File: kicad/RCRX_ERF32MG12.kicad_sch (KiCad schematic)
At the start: 98 parts

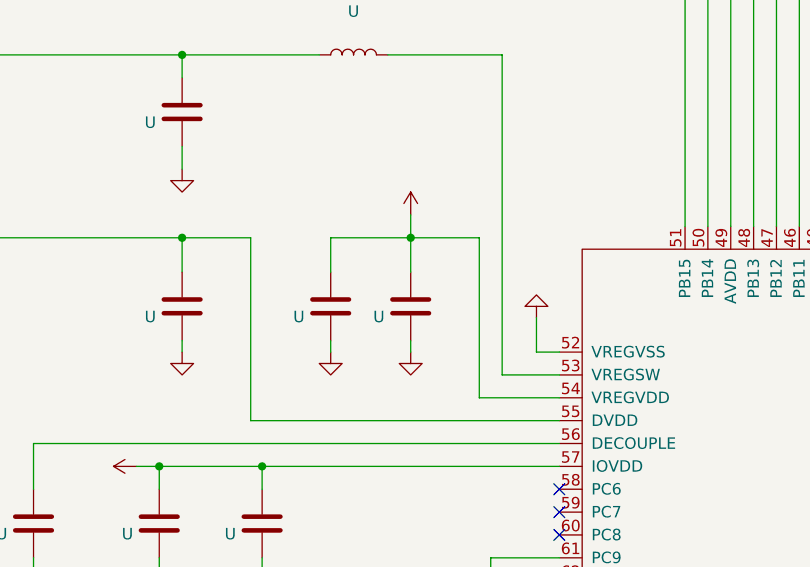
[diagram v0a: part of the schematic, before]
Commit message: Adding PIB USB BRIDGE UML state diagrams
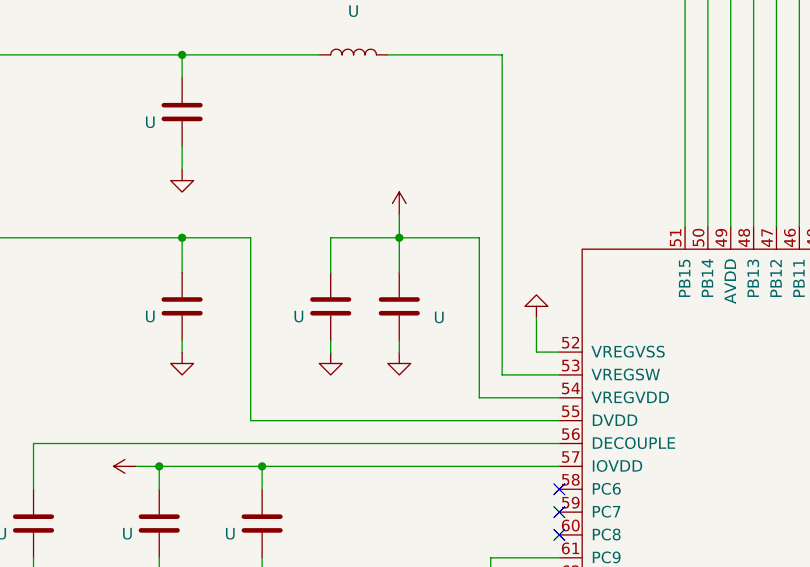
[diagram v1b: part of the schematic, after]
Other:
- moved on the sheet: U

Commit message: Adding PIB USB BRIDGE UML state diagrams - WIP
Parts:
- removed J: Conn_01x02, symbol Connector_Generic:Conn_01x02
- removed U: (no value), symbol device:C
- removed U: (no value), symbol device:R
- added J1: BUZZER, symbol Connector_Generic:Conn_01x02
- C? (x3): renamed from U; value (none) -> 13p
- C? (x2): renamed from U; value (none) -> 33p
- C? (x2): renamed from U; value (none) -> 43p
- C? (x2): renamed from U; value (none) -> 2.2p
- C?: renamed from U; value (none) -> 1p
- C?: renamed from U; value (none) -> 3p
- C? (x8): renamed from U; value (none) -> 100n
- C? (x2): renamed from U; value (none) -> 56p
- C? (x2): renamed from U; value (none) -> 10p
- C?, L?: renamed from U; value (none) -> 220n
- C? (x3), L?: renamed from U; value (none) -> 4u7
- C? (x6): renamed from U; value (none) -> 1u
- C? (x2): renamed from U; value (none) -> 10u
- C?: renamed from U; value (none) -> 10n
- C? (x2): renamed from U; value (none) -> 1n
- C? (x6): renamed from U; value (none) -> 100p
- C? (x2): renamed from U; value (none) -> 68p
- D?: renamed from U; value (none) -> D_Schottky
- HEX_SW?: renamed from U; value (none) -> RF_BAND_SEL
- HEX_SW?: renamed from U; value (none) -> MODEL_ID
- J?: renamed from U; value (none) -> USB_OTG
- J?: renamed from U; value (none) -> Micro_SD_Card
- J?: renamed from U; value (none) -> 50 Ohm 430-460 MHz Antenna
- J?: renamed from U; value (none) -> 50 Ohm 13-79 MHz Antenna
- J?: renamed from U; value (none) -> 50 Ohm 2.4 GHz Antenna
- L?: renamed from U; value (none) -> CBF102WB
- L? (x2): renamed from U; value (none) -> 390n
- L? (x2): renamed from U; value (none) -> 3n
- L? (x2): renamed from U; value (none) -> 62n
- L?: renamed from U; value (none) -> 130n
- L? (x2): renamed from U; value (none) -> 82n
- L? (x2): renamed from U; value (none) -> 470n
- L? (x2): renamed from U; value (none) -> BLM18AG601SN1
- L? (x2): renamed from U; value (none) -> L
- L? (x3): renamed from U; value (none) -> 180n
- L?: renamed from U; value (none) -> 36n
- P?: renamed from U; value (none) -> I2C_BUS
- P?: renamed from U; value (none) -> BATT
- P?: renamed from U; value (none) -> CRSF_BUS
- P?: renamed from U; value (none) -> Nokia 5110 display
- Q?: renamed from U; value (none) -> Q_PMOS_DGS
- R?: renamed from U; value (none) -> 100k
- R?: renamed from U; value (none) -> 1R
- SW?: renamed from U; value (none) -> RESET
- U?: renamed from U; value (none) -> EFR32MG12P433F1024GM48; footprint (none) -> Footprint
- U?: renamed from U; value (none) -> PIC16(L)F1459-I_ML
- U?: renamed from U; value (none) -> LM1117-5.0
- U?: renamed from U; value (none) -> LM1117-3.3
- U? (x2): renamed from U; value (none) -> TLV70245_SOT23-5; footprint (none) -> TO_SOT_Packages_SMD:SOT-23-5
- U? (x2): renamed from U; value (none) -> MAX2650; footprint (none) -> smd-semi:SOT-143
- U?: renamed from U; value (none) -> ADE-1+; footprint (none) -> RF_Mini-Circuits:Mini-Circuits_CD542_LandPatternPL-052
- Y?: renamed from U; value (none) -> 38.400 MHz
- Y?: renamed from U; value (none) -> 514CCAXXXXXXCAG; footprint (none) -> Si500D
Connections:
- net +3V3: now also J?.4 (VDD), P?.1 (Pin_1)
- net BUZZER: now also U?.12 (RC1), U?.59 (PC7), J1.1 (Pin_1)
- net GND: now also J1.2 (Pin_2)
- net /SD_CE: now also U?.60 (PC8); no longer U?.61 (PC9)
- net at J?.2 (D-), U?.15 (D-): no longer U?.12 (RC1)
- net at J?.3 (D+), U?.16 (D+): no longer U?.13 (RC0)
- net at C?.2, U?.14 (Vusb3v3): no longer J?.4 (VDD), P?.1 (Pin_1)
- net /LCD_RESET: now reaches P?.11 (Pin_11)
- net /LCD_RESET: now also U?.13 (RC0), U?.61 (PC9)
- no-connect marks 7 -> 5
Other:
- note added: "USB Adapter for: CMSIS-DAP / COM port / Mass storage (SD Card)"
- moved on the sheet: C?, D?, J?, P?, Q?, R?, SW?, U?

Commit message: Adding PIB USB BRIDGE UML state diagrams - WIP
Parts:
- removed C? (x2): 33p, symbol device:C
- removed C? (x2): 43p, symbol device:C
- removed C? (x2): 2.2p, symbol device:C
- removed C?: 1p, symbol device:C
- removed C? (x2): 56p, symbol device:C
- removed C? (x2): 68p, symbol device:C
- removed D?: D_Schottky, symbol device:D_Schottky
- removed J1: BUZZER, symbol Connector_Generic:Conn_01x02
- removed J?: USB_OTG, symbol conn:USB_OTG
- removed J?: Micro_SD_Card, symbol conn:Micro_SD_Card
- removed L? (x2): 3n, symbol device:L
- removed L? (x2): 62n, symbol device:L
- removed L?: 130n, symbol device:L
- removed L? (x2): 82n, symbol device:L
- removed L? (x3): 180n, symbol device:L
- removed P?: Nokia 5110 display, symbol conn:Conn_02x06_Odd_Even
- removed Q?: Q_PMOS_DGS, symbol device:Q_PMOS_DGS
- removed R?: 100k, symbol device:R
- removed SW?: RESET, symbol RCTX-rescue:SW_Push-switches
- removed U?: PIC16(L)F1459-I_ML, symbol PIC_USB_BRIDGE:PIC16(L)F1459-I_ML
- added C1, C2: 33p, symbol device:C
- added D1: D_Schottky, symbol device:D_Schottky
- added J21: BUZZER, symbol Connector_Generic:Conn_01x02
- added J22: USB_OTG, symbol conn:USB_OTG
- added P1: Nokia 5110 display, symbol conn:Conn_02x06_Odd_Even
- added P?: SD Card, symbol conn:Conn_02x05_Odd_Even
- added Q1: Q_PMOS_DGS, symbol device:Q_PMOS_DGS
- added R1: 100k, symbol device:R
- added SW1: RESET, symbol RCTX-rescue:SW_Push-switches
- added U1: PIC16(L)F1459-I_ML, symbol PIC_USB_BRIDGE:PIC16(L)F1459-I_ML
- added U?: RLP-83+, symbol RF:RLP-83+
- added U?: RBP-440+, symbol RF:RBP-440+
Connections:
- net +3V3: now also P1.1 (Pin_1), P?.1 (Pin_1)
- net +5V: now also Q1.1 (D)
- net BUZZER: now also U?.63 (PC11), J21.1 (Pin_1), U1.20 (RA4); no longer U?.48 (PB13), U?.59 (PC7)
- net GND: now also C1.1, C2.2, J21.2 (Pin_2), J22.6 (Shield), P1.10 (Pin_10), P1.12 (Pin_12), P1.2 (Pin_2), P1.4 (Pin_4), P1.6 (Pin_6), P1.8 (Pin_8), P?.10 (Pin_10), P?.2 (Pin_2), P?.4 (Pin_4), P?.6 (Pin_6), P?.8 (Pin_8), R1.2, SW1.2, U1.17 (VSS), U?.1 (GND), U?.1 (GND), U?.2 (GND), U?.2 (GND), U?.3 (GND), U?.3 (GND), U?.5 (GND), U?.5 (GND), U?.6 (GND), U?.6 (GND), U?.7 (GND), U?.7 (GND)
- net LCD_D/C: now also P1.9 (Pin_9), U1.13 (RC0); no longer U?.63 (PC11)
- net SCK: now also P1.7 (Pin_7), P?.7 (Pin_7), U1.8 (SCK)
- net SDI: now also P?.5 (Pin_5), U1.10 (SDI)
- net SDO: now also P1.5 (Pin_5), P?.3 (Pin_3), U1.6 (SDO)
- net SOC_RESETn: now also U1.5 (RC6)
- net SWCLK: now also U1.2 (RC5)
- net SWDIO: now also U1.3 (RC4)
- net SWO: now also U1.4 (RC3)
- net USB_RX: now also U1.9 (RX)
- net USB_TX: now also U1.7 (TX)
- net /LCD_CE: now also P1.3 (Pin_3), U1.12 (RC1); no longer U?.62 (PC10)
- net /LCD_RESET: now also P1.11 (Pin_11), U1.19 (RA5); no longer U?.61 (PC9)
- net /SD_CE: now also P?.9 (Pin_9), U1.11 (RC2); no longer U?.60 (PC8)
- net at J?.1 (In): now also U?.4 (RF) (x2)
- net at C?.1, C?.2: now also U?.8 (RF), U?.8 (RF)
- new net: D1.2 (A), J22.5 (GND), Q1.2 (G), R1.1
- new net: J22.1 (VBUS), SW1.1, U1.1 (Vpp)
- new net: C1.2, U1.14 (Vusb3v3)
- new net: J22.2 (D-), U1.15 (D-)
- new net: J22.3 (D+), U1.16 (D+)
- new net: C2.1, D1.1 (K), Q1.3 (S), U1.18 (VDD)
- no-connect marks 5 -> 8
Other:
- note added: "- UART bridge for SD card and Nokia 5110 LCD - USB Adapter for: CMSIS-DAP / COM port / Mass storage (SD Card)"
- note added: "2.4 GHz band filter"
- note added: "HF/VHF band filter"
- note added: "RX and TX frontend power"
- note added: "SDO"
- note added: "SD_CARD SS/CS"
- note added: "Sub-GHz multiband 110 MHz up-down converter, pre-amp and power-amp RF MHz ± LO MHz -> IF MHz ------------------------ 10 ... 80 + 110 -> 120-190 430 ... 460 - 110 -> 320-350"
- note added: "UHF band filter"
- note removed: "High Band harmonics suppressor 5th order Chebyshev band pass filter fc: 400-500 MHz"
- note removed: "Low Band harmonics suppressor 9th order Chebyshev low pass filter fc: 80 MHz"
- note removed: "USB Adapter for: CMSIS-DAP / COM port / Mass storage (SD Card)"
- moved on the sheet: C?, J?, L?, U?, Y?

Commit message: Adding PIC docs
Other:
- note added: "- UART bridge for SD card and Nokia 5110 LCD - USB Adapter for: CMSIS-DAP / COM port / MSD (SD Card)"
- note removed: "- UART bridge for SD card and Nokia 5110 LCD - USB Adapter for: CMSIS-DAP / COM port / Mass storage (SD Card)"
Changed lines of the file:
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@@
     (stroke (width 0) (type default))
   )
-  (wire (pts (xy 153.67 229.87) (xy 168.91 229.87))
+  (wire (pts (xy 153.67 229.87) (xy 167.64 229.87))
     (stroke (width 0) (type default))
   )
@@
     (stroke (width 0) (type default))
   )
-  (wire (pts (xy 153.67 234.95) (xy 168.91 234.95))
+  (wire (pts (xy 153.67 234.95) (xy 167.64 234.95))
     (stroke (width 0) (type default))
   )
@@
     (effects (font (size 1.27 1.27)) (justify left bottom))
   )
-  (text "- UART bridge for SD card and Nokia 5110 LCD\n- USB Adapter for: CMSIS-DAP / COM port / Mass storage (SD Card)"
+  (text "- UART bridge for SD card and Nokia 5110 LCD\n- USB Adapter for: CMSIS-DAP / COM port / MSD (SD Card)"
     (at 13.97 194.31 0)
     (effects (font (size 1.27 1.27)) (justify left bottom))
@@
     )
   )
-  (global_label "USB_RX" (shape input) (at 168.91 229.87 0)
-    (effects (font (size 1.27 1.27)) (justify left))
-    (property "Intersheetrefs" "${INTERSHEET_REFS}" (at 8.89 -2.54 0)
+  (global_label "USB_RX" (shape input) (at 167.64 229.87 0)
+    (effects (font (size 1.27 1.27)) (justify left))
+    (property "Intersheetrefs" "${INTERSHEET_REFS}" (at 7.62 -2.54 0)
       (effects (font (size 1.27 1.27)) hide)
     )
@@
     )
   )
-  (global_label "USB_TX" (shape output) (at 168.91 234.95 0)
-    (effects (font (size 1.27 1.27)) (justify left))
-    (property "Intersheetrefs" "${INTERSHEET_REFS}" (at 8.89 7.62 0)
-      (effects (font (size 1.27 1.27)) hide)
-    )
+  (global_label "USB_TX" (shape output) (at 167.64 234.95 0)
+    (effects (font (size 1.27 1.27)) (justify left))
+    (property "Intersheetrefs" "${INTERSHEET_REFS}" (at 7.62 7.62 0)
+      (effects (font (size 1.27 1.27)) hide)
+    )

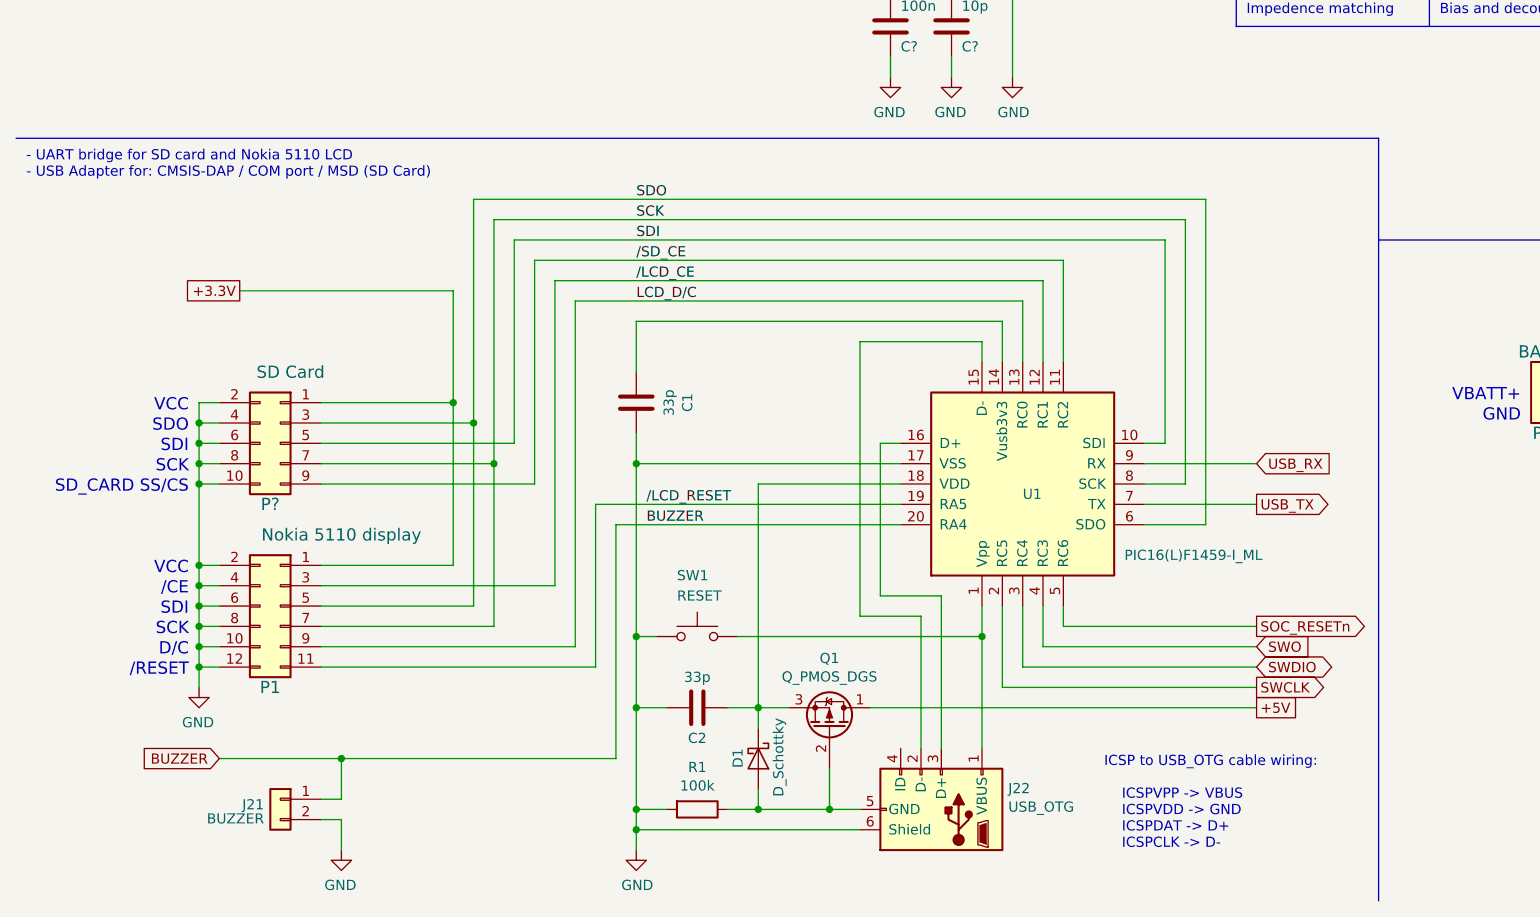
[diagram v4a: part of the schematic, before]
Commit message: Reset PIC by cutting off Vdd via a n/c SW instead of grounding the USB VBUS on Vpp via a n/o SW
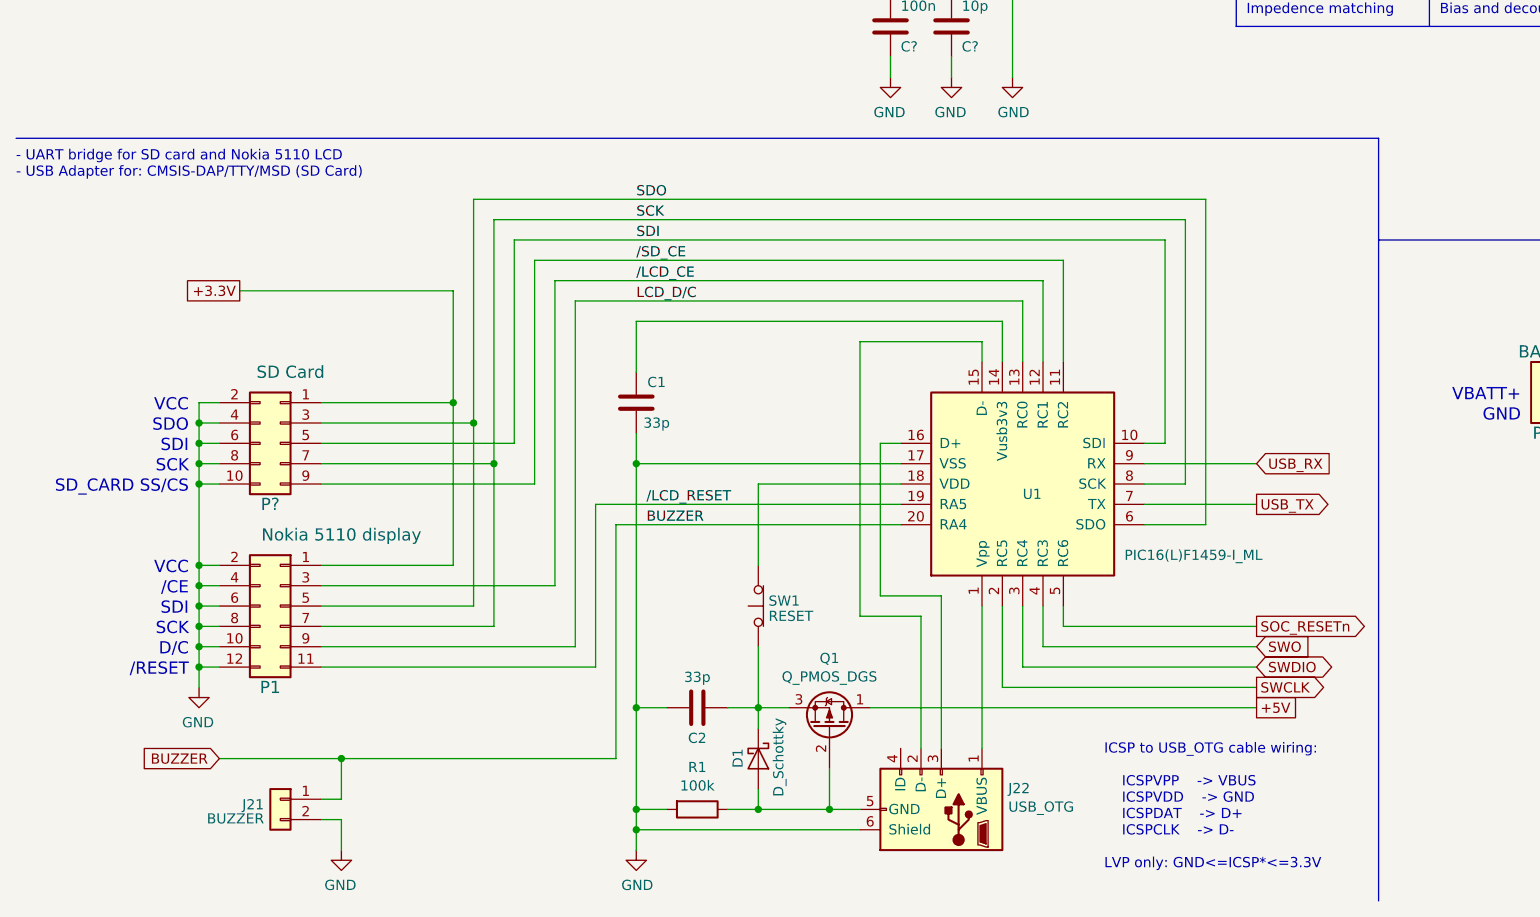
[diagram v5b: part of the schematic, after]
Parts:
- removed SW1: RESET, symbol RCTX-rescue:SW_Push-switches
- added SW1: RESET, symbol switches:SW_Push_Open
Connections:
- net at C2.1, D1.1 (K), Q1.3 (S): now also SW1.1 (A); no longer U1.18 (VDD)
- new net: SW1.2 (B), U1.18 (VDD)
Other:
- note added: "- UART bridge for SD card and Nokia 5110 LCD - USB Adapter for: CMSIS-DAP/TTY/MSD (SD Card)"
- note added: "ICSP to USB_OTG cable wiring: ICSPVPP -> VBUS ICSPVDD -> GND ICSPDAT -> D+ ICSPCLK -> D- LVP only: GND<=ICSP*<=3.3V"
- note removed: "- UART bridge for SD card and Nokia 5110 LCD - USB Adapter for: CMSIS-DAP / COM port / MSD (SD Card)"
- note removed: "ICSP to USB_OTG cable wiring: ICSPVPP -> VBUS ICSPVDD -> GND ICSPDAT -> D+ ICSPCLK -> D-"
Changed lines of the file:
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@@
   (junction (at 120.65 68.58) (diameter 0) (color 0 0 0 0)
   )
-  (junction (at 90.17 251.46) (diameter 0) (color 0 0 0 0)
-  )
   (junction (at 171.45 153.67) (diameter 0) (color 0 0 0 0)
   )
@@
   (junction (at 368.3 142.24) (diameter 0) (color 0 0 0 0)
   )
-  (junction (at 133.35 251.46) (diameter 0) (color 0 0 0 0)
-  )
   (junction (at 35.56 242.57) (diameter 0) (color 0 0 0 0)
   )
@@
     (stroke (width 0) (type default))
   )
-  (wire (pts (xy 90.17 251.46) (xy 90.17 260.35))
+  (wire (pts (xy 90.17 229.87) (xy 90.17 260.35))
     (stroke (width 0) (type default))
   )
@@
     (stroke (width 0) (type default))
   )
-  (wire (pts (xy 90.17 251.46) (xy 92.71 251.46))
-    (stroke (width 0) (type default))
-  )
   (wire (pts (xy 237.49 255.27) (xy 246.38 255.27))
     (stroke (width 0) (type default))
@@
     (stroke (width 0) (type default))
   )
+  (wire (pts (xy 105.41 252.73) (xy 105.41 260.35))
+    (stroke (width 0) (type default))
+  )
   (wire (pts (xy 73.66 93.98) (xy 73.66 90.17))
     (stroke (width 0) (type default))
@@
     (stroke (width 0) (type default))
   )
-  (wire (pts (xy 102.87 251.46) (xy 133.35 251.46))
-    (stroke (width 0) (type default))
-  )
   (wire (pts (xy 373.38 182.88) (xy 375.92 182.88))
     (stroke (width 0) (type default))
@@
     (stroke (width 0) (type default))
   )
-  (wire (pts (xy 90.17 229.87) (xy 90.17 251.46))
-    (stroke (width 0) (type default))
-  )
   (wire (pts (xy 118.11 41.91) (xy 124.46 41.91))
     (stroke (width 0) (type default))
@@
     (stroke (width 0) (type default))
   )
+  (wire (pts (xy 105.41 232.41) (xy 105.41 242.57))
+    (stroke (width 0) (type default))
+  )
   (wire (pts (xy 128.27 158.75) (xy 128.27 144.78))
     (stroke (width 0) (type default))
@@
     (stroke (width 0) (type default))
   )
-  (wire (pts (xy 133.35 265.43) (xy 133.35 251.46))
+  (wire (pts (xy 133.35 247.65) (xy 133.35 265.43))
     (stroke (width 0) (type default))
   )
@@
     (stroke (width 0) (type default))
   )
-  (wire (pts (xy 105.41 232.41) (xy 105.41 260.35))
-    (stroke (width 0) (type default))
-  )
   (wire (pts (xy 90.17 275.59) (xy 90.17 278.13))
     (stroke (width 0) (type default))
@@
     (stroke (width 0) (type default))
   )
-  (wire (pts (xy 133.35 251.46) (xy 133.35 247.65))
-    (stroke (width 0) (type default))
-  )
   (wire (pts (xy 368.3 140.97) (xy 368.3 142.24))
     (stroke (width 0) (type default))
@@
     (effects (font (size 1.27 1.27)) (justify left bottom))
   )
-  (text "- UART bridge for SD card and Nokia 5110 LCD\n- USB Adapter for: CMSIS-DAP / COM port / MSD (SD Card)"
-    (at 13.97 194.31 0)
+  (text "- UART bridge for SD card and Nokia 5110 LCD\n- USB Adapter for: CMSIS-DAP/TTY/MSD (SD Card)"
+    (at 12.7 194.31 0)
     (effects (font (size 1.27 1.27)) (justify left bottom))
   )
@@
     (effects (font (size 1.524 1.524)) (justify right bottom))
   )
-  (text "ICSP to USB_OTG cable wiring:\n\n    ICSPVPP -> VBUS \n    ICSPVDD -> GND  \n    ICSPDAT -> D+ \n    ICSPCLK -> D- "
-    (at 148.59 278.13 0)
+  (text "ICSP to USB_OTG cable wiring:\n\n    ICSPVPP	-> VBUS \n    ICSPVDD	-> GND  \n    ICSPDAT	-> D+ \n    ICSPCLK	-> D- \n\nLVP only: GND<=ICSP*<=3.3V"
+    (at 148.59 280.67 0)
     (effects (font (size 1.27 1.27)) (justify left bottom))
   )
@@
     )
   )
-  (symbol (lib_id "RCTX-rescue:SW_Push-switches") (at 97.79 251.46 0) (mirror y) (unit 1)
+  (symbol (lib_id "switches:SW_Push_Open") (at 105.41 247.65 90) (unit 1)
     (in_bom yes) (on_board yes) (dnp no)
-    (property "Reference" "SW1" (at 95.25 243.84 0)
+    (property "Reference" "SW1" (at 106.68 247.015 90)
       (effects (font (size 1.27 1.27)) (justify right))
     )
-    (property "Value" "RESET" (at 95.25 246.38 0)
+    (property "Value" "RESET" (at 106.68 248.92 90)
       (effects (font (size 1.27 1.27)) (justify right))
     )
-    (property "Footprint" "" (at 97.79 246.38 0)
+    (property "Footprint" "" (at 100.33 247.65 0)
       (effects (font (size 1.27 1.27)) hide)
     )
-    (property "Datasheet" "" (at 97.79 246.38 0)
+    (property "Datasheet" "" (at 100.33 247.65 0)
       (effects (font (size 1.27 1.27)) hide)
     )
@@
     (pin "2")
     (instances
-      (project "RCTX_ERF32MG12"
-        (path "/3ad7eac7-2269-4d5d-9588-a2093eccd000"
-          (reference "SW1") (unit 1)
-        )
-      )
       (project "RCRX_ERF32MG12"
         (path "/87bb696a-a669-4a90-8deb-639f039cb04c"
@@
   (symbol (lib_id "device:C") (at 90.17 222.25 180) (unit 1)
     (in_bom yes) (on_board yes) (dnp no)
-    (property "Reference" "C1" (at 96.5708 222.25 90)
+    (property "Reference" "C1" (at 92.71 219.71 0)
       (effects (font (size 1.27 1.27)))
     )
-    (property "Value" "33p" (at 94.2594 222.25 90)
+    (property "Value" "33p" (at 92.71 224.79 0)
       (effects (font (size 1.27 1.27)))
     )
